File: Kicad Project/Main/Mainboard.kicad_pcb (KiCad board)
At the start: 2 copper layers, 112.8 x 71.1 mm, 109 parts, among them J1 ICSP, P1 CONN_01X02, P2 USB_A, U1 ATmega328P, U10 MCP73871, U11 MCP73871, U12 Button_SPST_4, U13 3.5mm-Male-TH, U14 3.5mm-Female-TH, U2 LTC6800, U3 LTC6800, U4 ADS1015, U5 LTC3114-1, U6 SM72238, U7 LM75BDP, U8 HIH6130, U9 FT232R, X1 32kHz

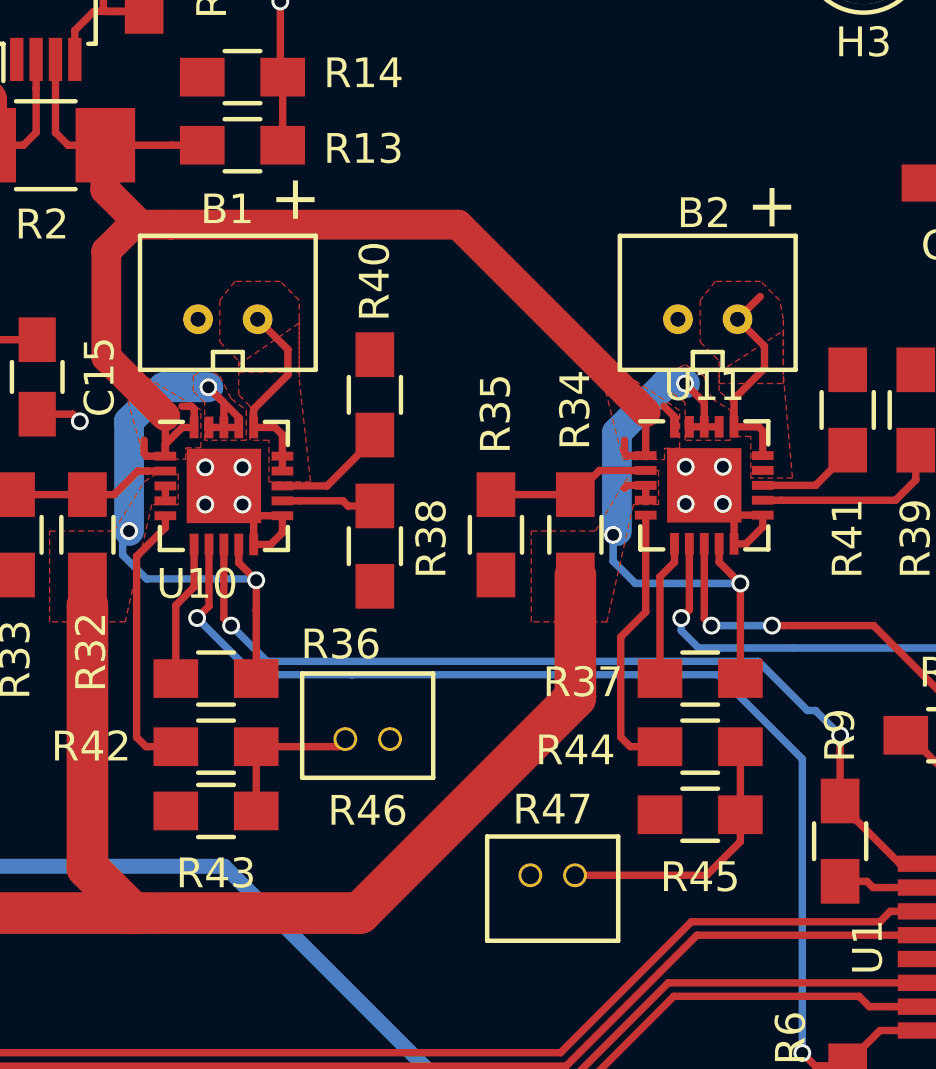
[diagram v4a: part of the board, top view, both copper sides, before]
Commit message: Edited JST footprints and updated board Small edits to READM
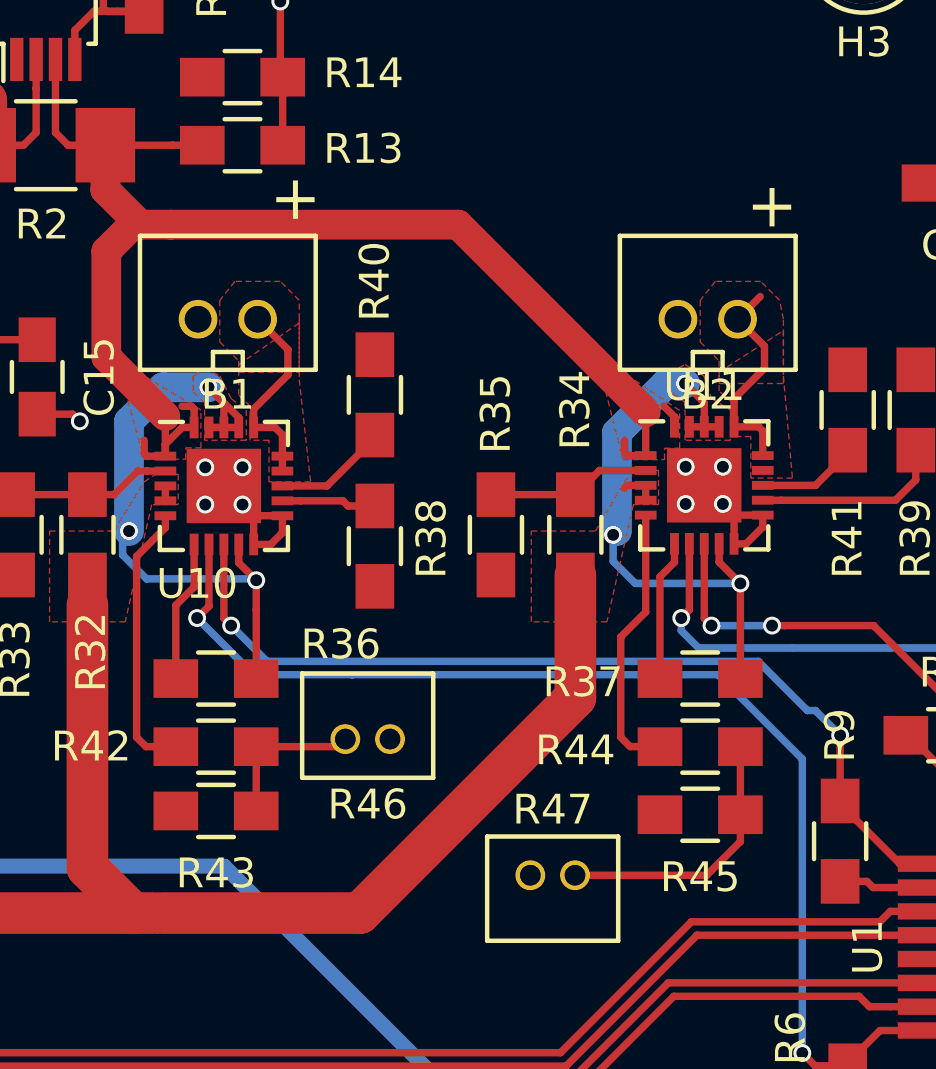
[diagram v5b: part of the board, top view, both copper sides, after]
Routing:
- added copper zone on F.Cu, net Net-(C16-Pad1)
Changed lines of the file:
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@@
     (links 280)
     (no_connects 1)
-    (area 141.252619 46.005 258.161952 127.16)
+    (area 130.124287 46.005 268.655715 132.240001)
     (thickness 1.6)
     (drawings 31)
@@
     )
   )
-  (module RFCx:JST-1.5mm (layer F.Cu)
-    (at 198.755 85.852 180)
-    (fp_text reference R47 (at 0 2.2 180) (layer F.SilkS)
-      (effects (font (size 1 1) (thickness 0.15)))
-    )
-    (fp_text value NTC (at 0 -3.2 180) (layer F.Fab)
-      (effects (font (size 1 1) (thickness 0.15)))
-    )
-    (fp_line (start -2.2 1.3) (end -2.2 -2.2) (layer F.SilkS) (width 0.15))
-    (fp_line (start 2.2 1.3) (end 2.2 -2.2) (layer F.SilkS) (width 0.15))
-    (fp_line (start -2.2 -2.2) (end 2.2 -2.2) (layer F.SilkS) (width 0.15))
-    (fp_line (start -2.2 1.3) (end 2.2 1.3) (layer F.SilkS) (width 0.15))
-    (pad 1 thru_hole circle (at -0.75 0 180) (size 0.8 0.8) (drill 0.6) (layers *.Cu *.Mask F.SilkS)
-      (net 75 "Net-(R44-Pad2)"))
-    (pad 2 thru_hole circle (at 0.75 0 180) (size 0.8 0.8) (drill 0.6) (layers *.Cu *.Mask F.SilkS)
-      (net 1 GND))
-  )
   (module Capacitors_SMD:C_0805_HandSoldering (layer F.Cu)
     (at 158.3055 85.725 180)
@@
       (net 1 GND))
   )
-  (module RFCx:JST-2mm (layer F.Cu)
-    (at 187.849 67.183)
-    (fp_text reference B1 (at -0.016 -3.683) (layer F.SilkS)
-      (effects (font (size 1 1) (thickness 0.15)))
-    )
-    (fp_text value Li-ion-2Cell-Conn (at 0 -3.81) (layer F.Fab)
-      (effects (font (size 1 1) (thickness 0.15)))
-    )
-    (fp_line (start 0.5 1.1) (end 0.5 1.7) (layer F.SilkS) (width 0.15))
-    (fp_line (start -0.5 1.1) (end 0.5 1.1) (layer F.SilkS) (width 0.15))
-    (fp_line (start -0.5 1.7) (end -0.5 1.1) (layer F.SilkS) (width 0.15))
-    (fp_line (start -2.95 -2.8) (end -2.95 1.7) (layer F.SilkS) (width 0.15))
-    (fp_line (start 2.95 -2.8) (end 2.95 1.7) (layer F.SilkS) (width 0.15))
-    (fp_line (start -2.95 -2.8) (end 2.95 -2.8) (layer F.SilkS) (width 0.15))
-    (fp_line (start -2.95 1.7) (end 2.95 1.7) (layer F.SilkS) (width 0.15))
-    (pad 1 thru_hole circle (at -1 0) (size 1 1) (drill 0.5) (layers *.Cu *.Mask F.SilkS)
-      (net 1 GND))
-    (pad 2 thru_hole circle (at 1 0) (size 1 1) (drill 0.5) (layers *.Cu *.Mask F.SilkS)
-      (net 47 "Net-(B1-Pad2)"))
-  )
-  (module RFCx:JST-2mm (layer F.Cu)
-    (at 203.962 67.183)
-    (fp_text reference B2 (at -0.127 -3.556) (layer F.SilkS)
-      (effects (font (size 1 1) (thickness 0.15)))
-    )
-    (fp_text value Li-ion-2Cell-Conn (at 0 -3.81) (layer F.Fab)
-      (effects (font (size 1 1) (thickness 0.15)))
-    )
-    (fp_line (start 0.5 1.1) (end 0.5 1.7) (layer F.SilkS) (width 0.15))
-    (fp_line (start -0.5 1.1) (end 0.5 1.1) (layer F.SilkS) (width 0.15))
-    (fp_line (start -0.5 1.7) (end -0.5 1.1) (layer F.SilkS) (width 0.15))
-    (fp_line (start -2.95 -2.8) (end -2.95 1.7) (layer F.SilkS) (width 0.15))
-    (fp_line (start 2.95 -2.8) (end 2.95 1.7) (layer F.SilkS) (width 0.15))
-    (fp_line (start -2.95 -2.8) (end 2.95 -2.8) (layer F.SilkS) (width 0.15))
-    (fp_line (start -2.95 1.7) (end 2.95 1.7) (layer F.SilkS) (width 0.15))
-    (pad 1 thru_hole circle (at -1 0) (size 1 1) (drill 0.5) (layers *.Cu *.Mask F.SilkS)
-      (net 1 GND))
-    (pad 2 thru_hole circle (at 1 0) (size 1 1) (drill 0.5) (layers *.Cu *.Mask F.SilkS)
-      (net 48 "Net-(B2-Pad2)"))
-  )
   (module Resistors_SMD:R_0805_HandSoldering (layer F.Cu)
     (at 174.371 110.109 270)
@@
     )
   )
-  (module RFCx:JST-1.5mm (layer F.Cu)
-    (at 192.544 81.28)
-    (fp_text reference R46 (at 0 2.413) (layer F.SilkS)
-      (effects (font (size 1 1) (thickness 0.15)))
-    )
-    (fp_text value NTC (at 0 -3.2) (layer F.Fab)
-      (effects (font (size 1 1) (thickness 0.15)))
-    )
-    (fp_line (start -2.2 1.3) (end -2.2 -2.2) (layer F.SilkS) (width 0.15))
-    (fp_line (start 2.2 1.3) (end 2.2 -2.2) (layer F.SilkS) (width 0.15))
-    (fp_line (start -2.2 -2.2) (end 2.2 -2.2) (layer F.SilkS) (width 0.15))
-    (fp_line (start -2.2 1.3) (end 2.2 1.3) (layer F.SilkS) (width 0.15))
-    (pad 1 thru_hole circle (at -0.75 0) (size 0.8 0.8) (drill 0.6) (layers *.Cu *.Mask F.SilkS)
-      (net 73 "Net-(R42-Pad2)"))
-    (pad 2 thru_hole circle (at 0.75 0) (size 0.8 0.8) (drill 0.6) (layers *.Cu *.Mask F.SilkS)
-      (net 1 GND))
-  )
   (module Housings_QFP:TQFP-32_7x7mm_Pitch0.8mm (layer F.Cu)
     (at 215.392 88.265 90)
@@
       (net 1 GND))
   )
+  (module RFCx:JST-2mm (layer F.Cu)
+    (at 187.849 67.183)
+    (fp_text reference B1 (at 0 2.54) (layer F.SilkS)
+      (effects (font (size 1 1) (thickness 0.15)))
+    )
+    (fp_text value Li-ion-2Cell-Conn (at 0 -3.81) (layer F.Fab)
+      (effects (font (size 1 1) (thickness 0.15)))
+    )
+    (fp_line (start 0.5 1.1) (end 0.5 1.7) (layer F.SilkS) (width 0.15))
+    (fp_line (start -0.5 1.1) (end 0.5 1.1) (layer F.SilkS) (width 0.15))
+    (fp_line (start -0.5 1.7) (end -0.5 1.1) (layer F.SilkS) (width 0.15))
+    (fp_line (start -2.95 -2.8) (end -2.95 1.7) (layer F.SilkS) (width 0.15))
+    (fp_line (start 2.95 -2.8) (end 2.95 1.7) (layer F.SilkS) (width 0.15))
+    (fp_line (start -2.95 -2.8) (end 2.95 -2.8) (layer F.SilkS) (width 0.15))
+    (fp_line (start -2.95 1.7) (end 2.95 1.7) (layer F.SilkS) (width 0.15))
+    (pad 1 thru_hole circle (at -1 0) (size 1.3 1.3) (drill 0.9) (layers *.Cu *.Mask F.SilkS)
+      (net 1 GND))
+    (pad 2 thru_hole circle (at 1 0) (size 1.3 1.3) (drill 0.9) (layers *.Cu *.Mask F.SilkS)
+      (net 47 "Net-(B1-Pad2)"))
+  )
+  (module RFCx:JST-2mm (layer F.Cu)
+    (at 203.962 67.183)
+    (fp_text reference B2 (at 0 2.54) (layer F.SilkS)
+      (effects (font (size 1 1) (thickness 0.15)))
+    )
+    (fp_text value Li-ion-2Cell-Conn (at 0 -3.81) (layer F.Fab)
+      (effects (font (size 1 1) (thickness 0.15)))
+    )
+    (fp_line (start 0.5 1.1) (end 0.5 1.7) (layer F.SilkS) (width 0.15))
+    (fp_line (start -0.5 1.1) (end 0.5 1.1) (layer F.SilkS) (width 0.15))
+    (fp_line (start -0.5 1.7) (end -0.5 1.1) (layer F.SilkS) (width 0.15))
+    (fp_line (start -2.95 -2.8) (end -2.95 1.7) (layer F.SilkS) (width 0.15))
+    (fp_line (start 2.95 -2.8) (end 2.95 1.7) (layer F.SilkS) (width 0.15))
+    (fp_line (start -2.95 -2.8) (end 2.95 -2.8) (layer F.SilkS) (width 0.15))
+    (fp_line (start -2.95 1.7) (end 2.95 1.7) (layer F.SilkS) (width 0.15))
+    (pad 1 thru_hole circle (at -1 0) (size 1.3 1.3) (drill 0.9) (layers *.Cu *.Mask F.SilkS)
+      (net 1 GND))
+    (pad 2 thru_hole circle (at 1 0) (size 1.3 1.3) (drill 0.9) (layers *.Cu *.Mask F.SilkS)
+      (net 48 "Net-(B2-Pad2)"))
+  )
+  (module RFCx:JST-1.5mm (layer F.Cu)
+    (at 192.544 81.28)
+    (fp_text reference R46 (at 0 2.2) (layer F.SilkS)
+      (effects (font (size 1 1) (thickness 0.15)))
+    )
+    (fp_text value NTC (at 0 -3.2) (layer F.Fab)
+      (effects (font (size 1 1) (thickness 0.15)))
+    )
+    (fp_line (start -2.2 1.3) (end -2.2 -2.2) (layer F.SilkS) (width 0.15))
+    (fp_line (start 2.2 1.3) (end 2.2 -2.2) (layer F.SilkS) (width 0.15))
+    (fp_line (start -2.2 -2.2) (end 2.2 -2.2) (layer F.SilkS) (width 0.15))
+    (fp_line (start -2.2 1.3) (end 2.2 1.3) (layer F.SilkS) (width 0.15))
+    (pad 1 thru_hole circle (at -0.75 0) (size 1 1) (drill 0.7) (layers *.Cu *.Mask F.SilkS)
+      (net 73 "Net-(R42-Pad2)"))
+    (pad 2 thru_hole circle (at 0.75 0) (size 1 1) (drill 0.7) (layers *.Cu *.Mask F.SilkS)
+      (net 1 GND))
+  )
+  (module RFCx:JST-1.5mm (layer F.Cu)
+    (at 198.755 85.852 180)
+    (fp_text reference R47 (at 0 2.2 180) (layer F.SilkS)
+      (effects (font (size 1 1) (thickness 0.15)))
+    )
+    (fp_text value NTC (at 0 -3.2 180) (layer F.Fab)
+      (effects (font (size 1 1) (thickness 0.15)))
+    )
+    (fp_line (start -2.2 1.3) (end -2.2 -2.2) (layer F.SilkS) (width 0.15))
+    (fp_line (start 2.2 1.3) (end 2.2 -2.2) (layer F.SilkS) (width 0.15))
+    (fp_line (start -2.2 -2.2) (end 2.2 -2.2) (layer F.SilkS) (width 0.15))
+    (fp_line (start -2.2 1.3) (end 2.2 1.3) (layer F.SilkS) (width 0.15))
+    (pad 1 thru_hole circle (at -0.75 0 180) (size 1 1) (drill 0.7) (layers *.Cu *.Mask F.SilkS)
+      (net 75 "Net-(R44-Pad2)"))
+    (pad 2 thru_hole circle (at 0.75 0 180) (size 1 1) (drill 0.7) (layers *.Cu *.Mask F.SilkS)
+      (net 1 GND))
+  )
   (dimension 112.776 (width 0.3) (layer Cmts.User)
     (gr_text "4.4400 in" (at 198.628 130.89) (layer Cmts.User)
@@
     )
   )
-  (zone (net 7) (net_name +5V) (layer F.Cu) (hatch edge 0.508)
+  (zone (net 76) (net_name "Net-(C16-Pad1)") (layer F.Cu) (hatch edge 0.508)
     (priority 1)
     (connect_pads (clearance 0.1))

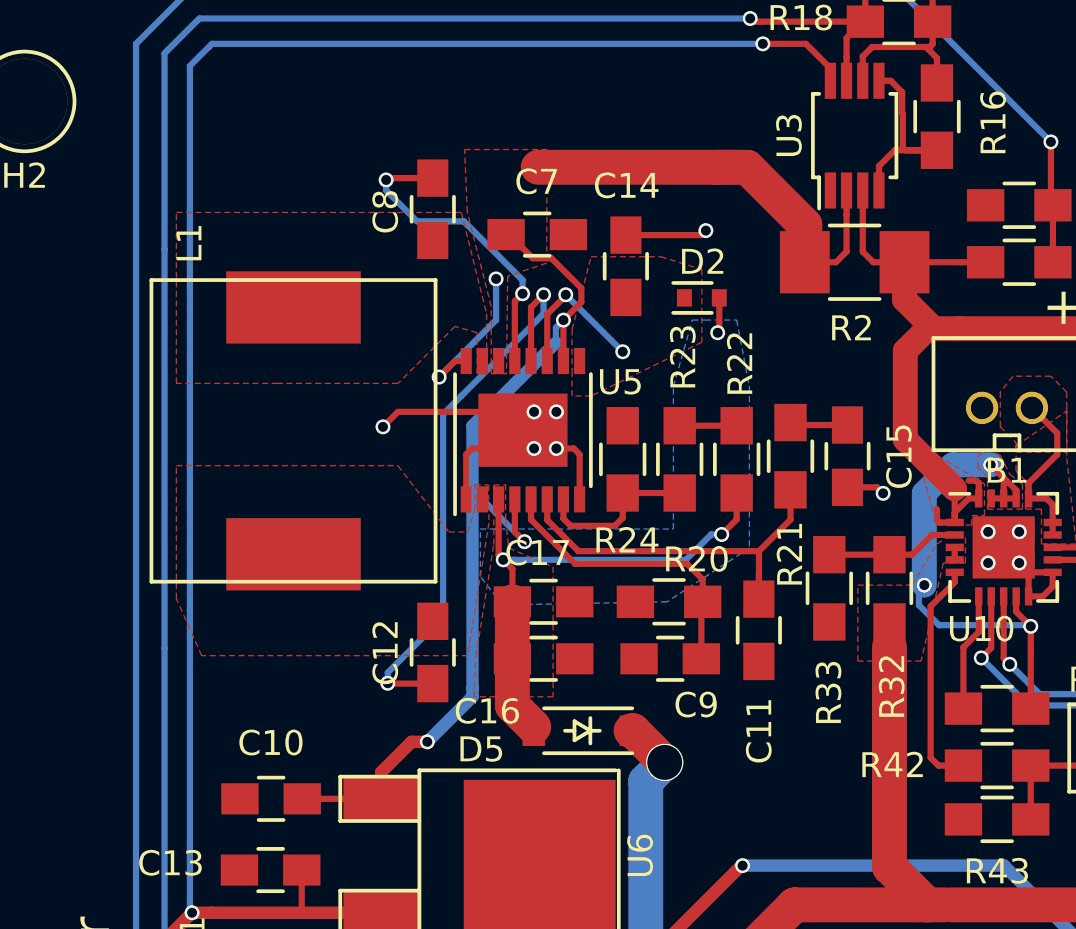
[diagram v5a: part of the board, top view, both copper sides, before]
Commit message: Replaced DC-DC Switching circuit with a prebuilt module
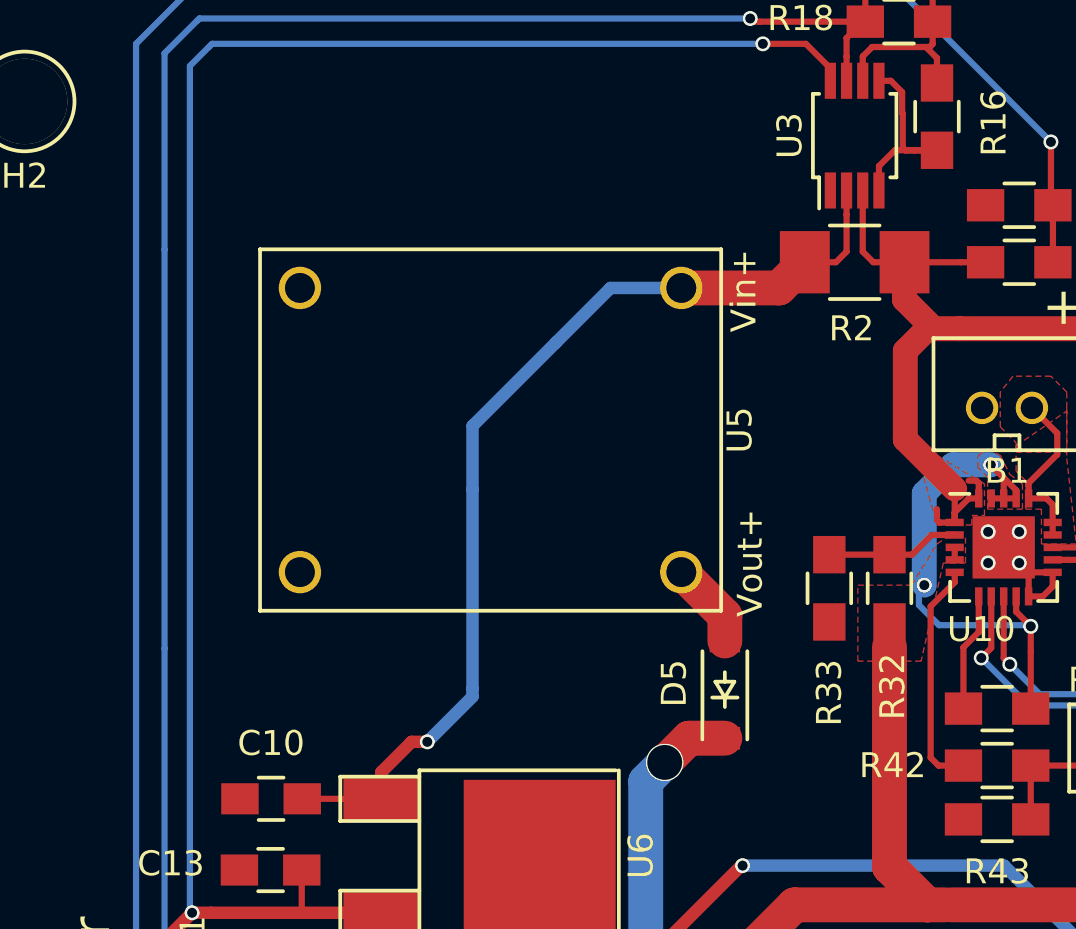
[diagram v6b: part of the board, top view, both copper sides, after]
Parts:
- removed C11: 10p, Capacitors_SMD:C_0805_HandSoldering
- removed C12, C8: 68nF, Capacitors_SMD:C_0805_HandSoldering
- removed C14: 4.7uF, Capacitors_SMD:C_0805_HandSoldering
- removed C15: 4700pF, Capacitors_SMD:C_0805_HandSoldering
- removed C16, C17: 22uF, Capacitors_SMD:C_0805_HandSoldering
- removed C7: 10uF, Capacitors_SMD:C_0805_HandSoldering
- removed C9: 10nF, Capacitors_SMD:C_0805_HandSoldering
- removed D2: PMEG2010AEB, Diodes_SMD:SOD-523
- removed G***: LOGO, Graphics:rfcx
- removed L1: 68uH, RFCx:Ind-Wurth-12_1x11_4
- removed R20: 21k, Resistors_SMD:R_0805_HandSoldering
- removed R21: 27.4k, Resistors_SMD:R_0805_HandSoldering
- removed R22: 49.9, Resistors_SMD:R_0805_HandSoldering
- removed R23: 2M, Resistors_SMD:R_0805_HandSoldering
- removed R24: 499k, Resistors_SMD:R_0805_HandSoldering
- removed REF**: Symbol_OSHW-Logo_SilkScreen, Symbols:Symbol_OSHW-Logo_SilkScreen
- U5: value LTC3114-1 -> DC-DC_Boost_Module; footprint Housings_SSOP:TSSOP-16-1EP_4.4x5mm_Pitch0.65mm -> RFCx:DC-DC_Boost_Module
- moved D5 5.95 mm to (176.5, 78.5), turned to 90 degrees
- moved U5 1.30 mm to (167.1, 68.1)
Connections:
- D5 pad 2: Net-(C16-Pad1) -> Net-(D5-Pad2)
- U5 pad 2: Net-(C12-Pad1) -> Net-(D5-Pad2)
- U5 pad 3: Net-(C16-Pad1) -> /ADC/Output-Current-L
- U5 pad 4: /ADC/Output-Current-L -> GND
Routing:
- net Net-(C12-Pad2): track 22.9 -> 0.00 mm, vias 2 -> 0
- net Net-(C16-Pad1): track 22.4 -> 0.00 mm, vias 3 -> 0
- net /ADC/Output-Current-L: track 62.4 -> 40.6 mm, vias 5 -> 1
- net GND: track 96.6 -> 77.5 mm, vias 29 -> 22
- net Net-(C11-Pad1): track 14.8 -> 0.00 mm
- net Net-(C8-Pad2): track 12.7 -> 0.00 mm, vias 2 -> 0
- net Net-(C9-Pad1): track 11.9 -> 0.00 mm
- net Net-(R23-Pad2): track 6.69 -> 0.00 mm
- net Net-(C14-Pad1): track 6.61 -> 0.00 mm, vias 2 -> 0
- net Net-(D5-Pad2): track 0.00 -> 3.49 mm
- net Net-(C15-Pad1): track 2.33 -> 0.00 mm
- net Net-(R22-Pad2): track 2.29 -> 0.00 mm
- net +5V: track 56.9 -> 57.8 mm
- removed copper zone on F.Cu, net /ADC/Output-Current-L
- removed copper zone on F.Cu, net Net-(C12-Pad1)
- removed copper zone on F.Cu, net Net-(C14-Pad1)
- removed copper zone on B.Cu, net Net-(C16-Pad1)
- removed copper zone on F.Cu, net Net-(C16-Pad1)
- removed copper zone on F.Cu, net Net-(C8-Pad1)
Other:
- board text added: "Vin+"
- board text added: "Vout+"
